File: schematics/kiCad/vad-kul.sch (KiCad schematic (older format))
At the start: 10 parts, among them J1 Lepton2Breakout, U1 RPIHeader

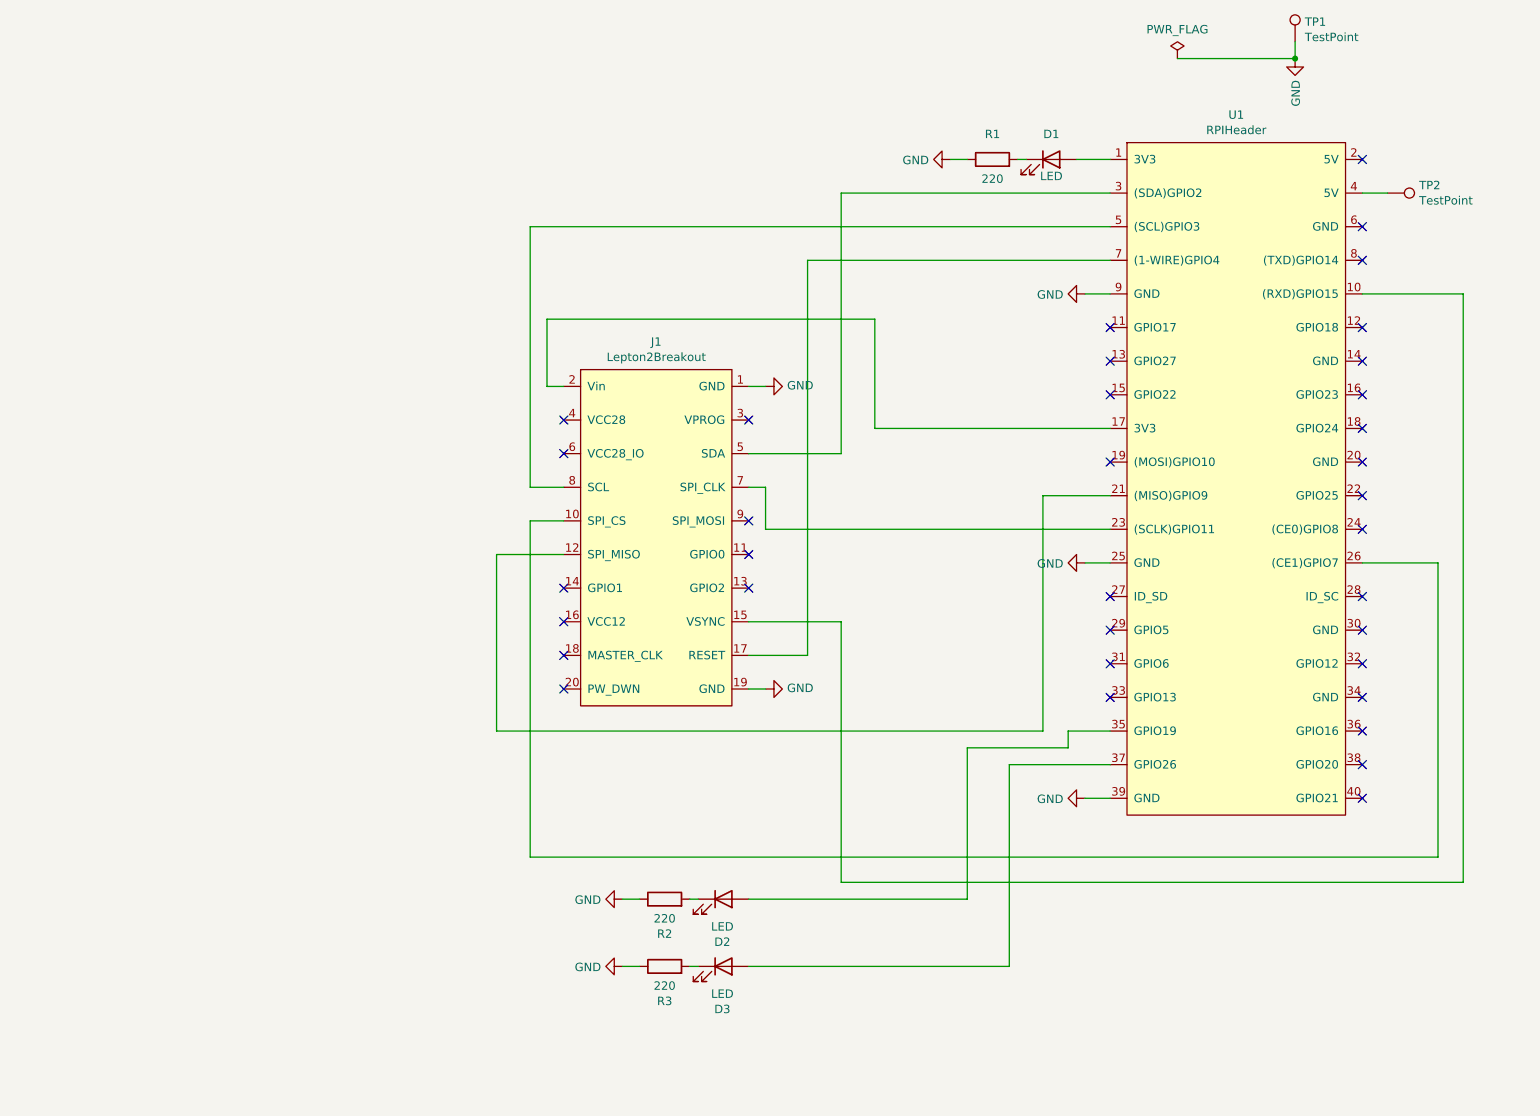
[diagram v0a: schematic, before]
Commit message: new pcb with sr04
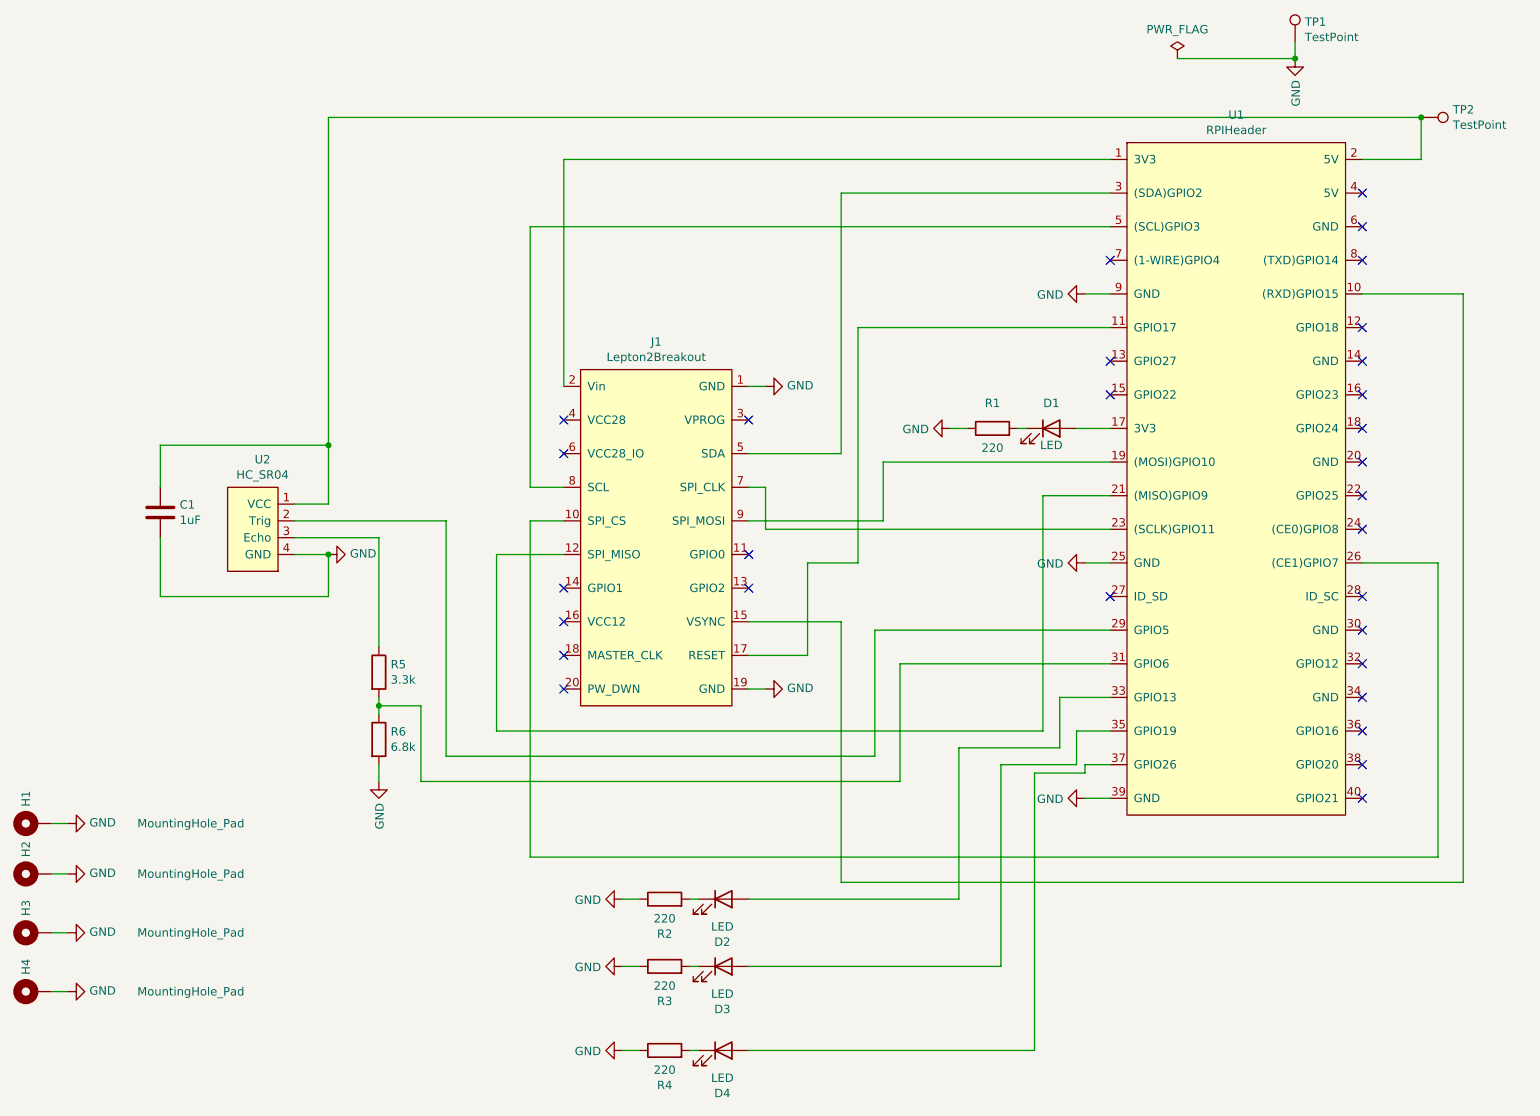
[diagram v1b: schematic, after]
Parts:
- added C1: 1uF, Capacitor_SMD:C_1206_3216Metric_Pad1.42x1.75mm_HandSolder, symbol Device:C
- added D4: LED, LED_THT:LED_D5.0mm, symbol Device:LED
- added H1, H2, H3, H4: MountingHole_Pad, MountingHole:MountingHole_2.7mm_M2.5_Pad, symbol Mechanical:MountingHole_Pad
- added R4: 220, Resistor_SMD:R_1206_3216Metric_Pad1.42x1.75mm_HandSolder, symbol Device:R
- added R5: 3.3k, Resistor_SMD:R_1206_3216Metric_Pad1.42x1.75mm_HandSolder, symbol Device:R
- added R6: 6.8k, Resistor_SMD:R_1206_3216Metric_Pad1.42x1.75mm_HandSolder, symbol Device:R
- added U2: HC_SR04, dmcginnis427Footprints:HC_SR04, symbol dmcginnis427:HC_SR04
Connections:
- net GND: now also C1.2, H1.1, H2.1, H3.1, H4.1, R4.1, R6.2, U2.4 (GND)
- net at D2.2 (A): now also U1.33 (GPIO13); no longer U1.35 (GPIO19)
- net at D3.2 (A): now also U1.35 (GPIO19); no longer U1.37 (GPIO26)
- net at J1.17 (RESET): now also U1.11 (GPIO17); no longer U1.7 ((1-WIRE)GPIO4)
- net at J1.2 (Vin): now also U1.1 (3V3); no longer U1.17 (3V3)
- net at J1.9 (SPI_MOSI): now also U1.19 ((MOSI)GPIO10)
- net at D1.2 (A): now also U1.17 (3V3); no longer U1.1 (3V3)
- net at U1.2 (5V): now also TP2.1, C1.1, U2.1 (VCC)
- net at U1.29 (GPIO5): now also U2.2 (Trig)
- net at U1.31 (GPIO6): now also R5.2, R6.1
- net at U1.4 (5V): no longer TP2.1
- new net: D4.2 (A), U1.37 (GPIO26)
- new net: R5.1, U2.3 (Echo)
- new net: D4.1 (K), R4.2
- no-connect marks 35 -> 30
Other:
- moved on the sheet: D1, R1, TP2
